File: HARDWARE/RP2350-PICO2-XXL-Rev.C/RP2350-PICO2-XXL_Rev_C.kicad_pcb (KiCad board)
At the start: 4 copper layers, 29 x 51 mm, 91 parts, among them Q1 Q12MHz/18pF/30ppm/4P/3.2x2.5m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, U1 W25Q128JVSIQ(SOIC-8_208mils), U2 TPS62A02ADRLR(SOT-563-6), U3 RP2350B(QFN-80_10.00x10.00x0.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, U4 NA(W25Q128JVSIQ(SOIC-8_208mil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, U5 APS6404L-3SQR-SN(SOIC-8_150mi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

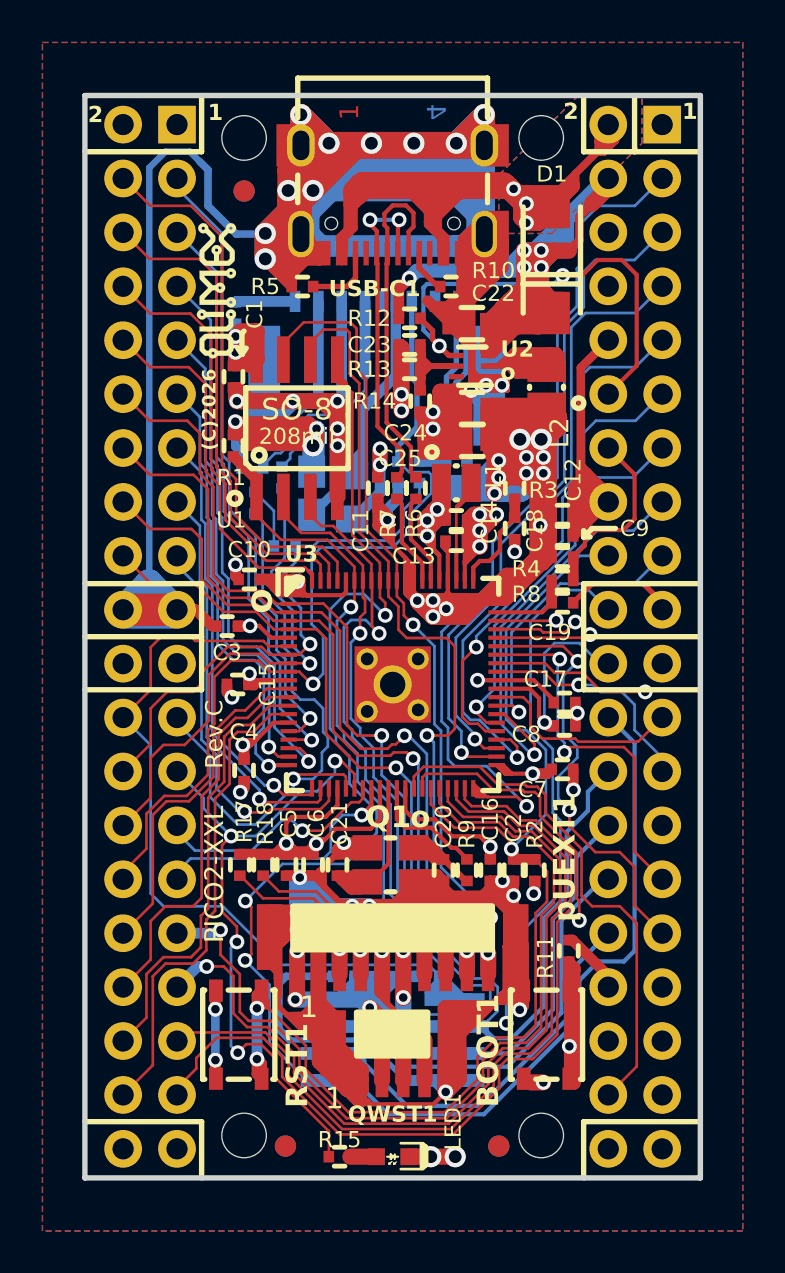
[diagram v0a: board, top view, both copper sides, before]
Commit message: removing unneeded connectors
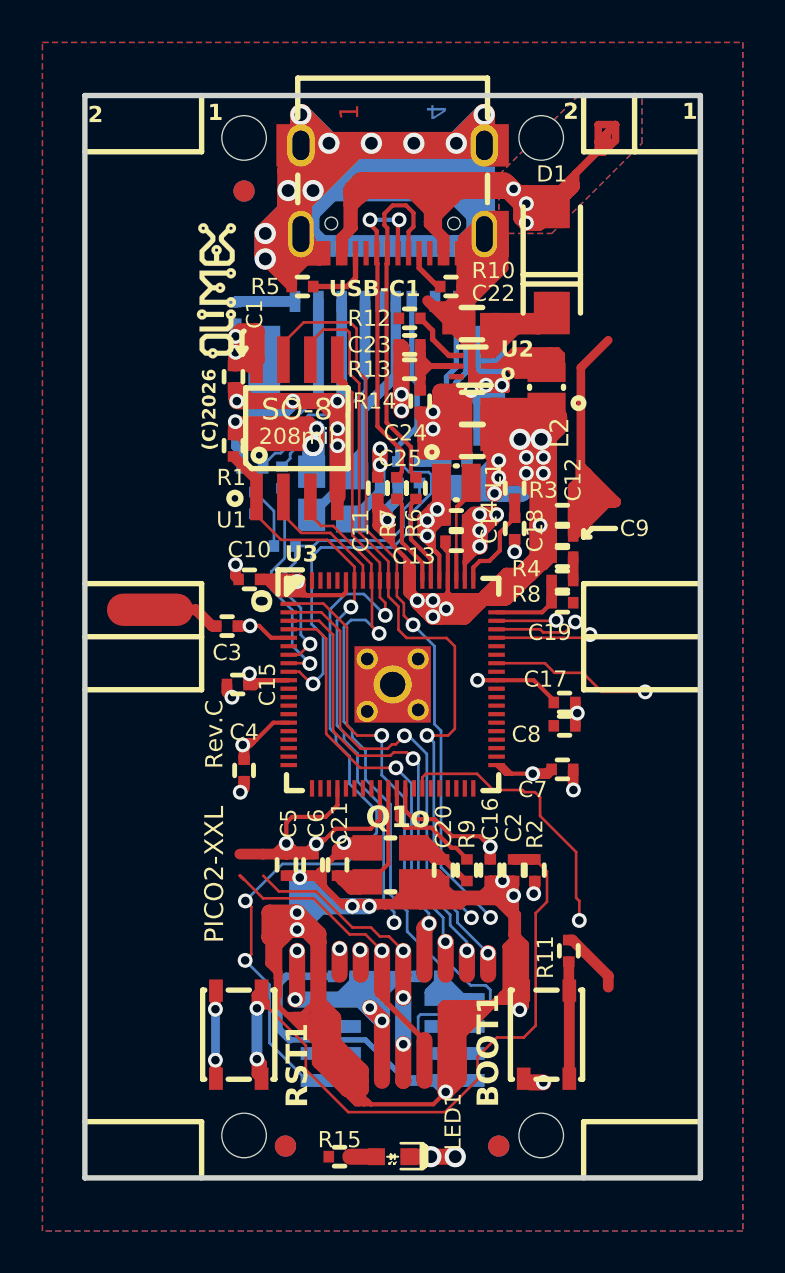
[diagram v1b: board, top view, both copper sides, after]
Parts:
- removed EXT1, EXT2: NA(HN2x20), OLIMEX_Connectors-FP:HN2x20
- removed QWST1: SH1.0-4P-180D, OLIMEX_Connectors-FP:BM04B-SRSS-TB
- removed R17, R18: 2.2k/R0402, OLIMEX_RLC-FP:R_0402_5MIL_DWS
- removed pUEXT1: SH1.0-10P-180D, OLIMEX_Connectors-FP:BM10B-SRSS-TB
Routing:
- net VSYS: track 62.9 -> 6.73 mm, vias 5 -> 0
- net /QSPI_SD1: track 52.0 -> 7.10 mm, vias 1 -> 0
- net /GPIO32: track 43.8 -> 0.00 mm, vias 1 -> 0
- net /BOOTSEL#: track 46.8 -> 5.53 mm, vias 2 -> 0
- net GND: track 634.6 -> 593.4 mm
- net /GPIO28: track 40.9 -> 0.00 mm, vias 1 -> 0
- net /GPIO29: track 40.2 -> 0.00 mm, vias 1 -> 0
- net /GPIO31: track 39.8 -> 0.00 mm
- net /GPIO30: track 38.0 -> 0.00 mm
- net /GPIO8\QMI_CS1n: track 40.1 -> 5.34 mm
- net /GPIO33: track 31.7 -> 0.00 mm, vias 1 -> 0
- net /GPIO25\User_Led: track 31.4 -> 0.00 mm, vias 4 -> 0
- net /QSPI_SD0: track 76.2 -> 46.0 mm
- net /GPIO16: track 29.5 -> 0.00 mm, vias 1 -> 0
- net /GPIO24\SPI1_RX\SD_DAT0: track 28.6 -> 0.00 mm, vias 1 -> 0
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
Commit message: cleaning up
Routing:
- net GND: track 593.4 -> 0.00 mm, vias 47 -> 0
- net +3.3V: track 385.8 -> 0.00 mm, vias 33 -> 0
- net /+1V1: track 112.2 -> 0.00 mm, vias 6 -> 0
- net VBUS: track 97.4 -> 0.00 mm, vias 3 -> 0
- net /GPIO3\I2C1_SCL: track 61.6 -> 0.00 mm, vias 1 -> 0
- net /GPIO2\I2C1_SDA: track 56.3 -> 0.00 mm, vias 3 -> 0
- net /GPIO47: track 47.5 -> 0.00 mm, vias 1 -> 0
- net /QSPI_SD0: track 46.0 -> 0.00 mm, vias 3 -> 0
- net /QSPI_CLK: track 44.1 -> 0.00 mm, vias 2 -> 0
- net /GPIO0\UART0_TX: track 44.0 -> 0.00 mm, vias 1 -> 0
- net /GPIO1\UART0_RX: track 43.7 -> 0.00 mm, vias 1 -> 0
- net /QSPI_CSn: track 42.0 -> 0.00 mm, vias 2 -> 0
- net /QSPI_SD3: track 41.7 -> 0.00 mm, vias 2 -> 0
- net /QSPI_SD2: track 38.7 -> 0.00 mm, vias 1 -> 0
- net /RUN: track 36.7 -> 0.00 mm, vias 2 -> 0
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
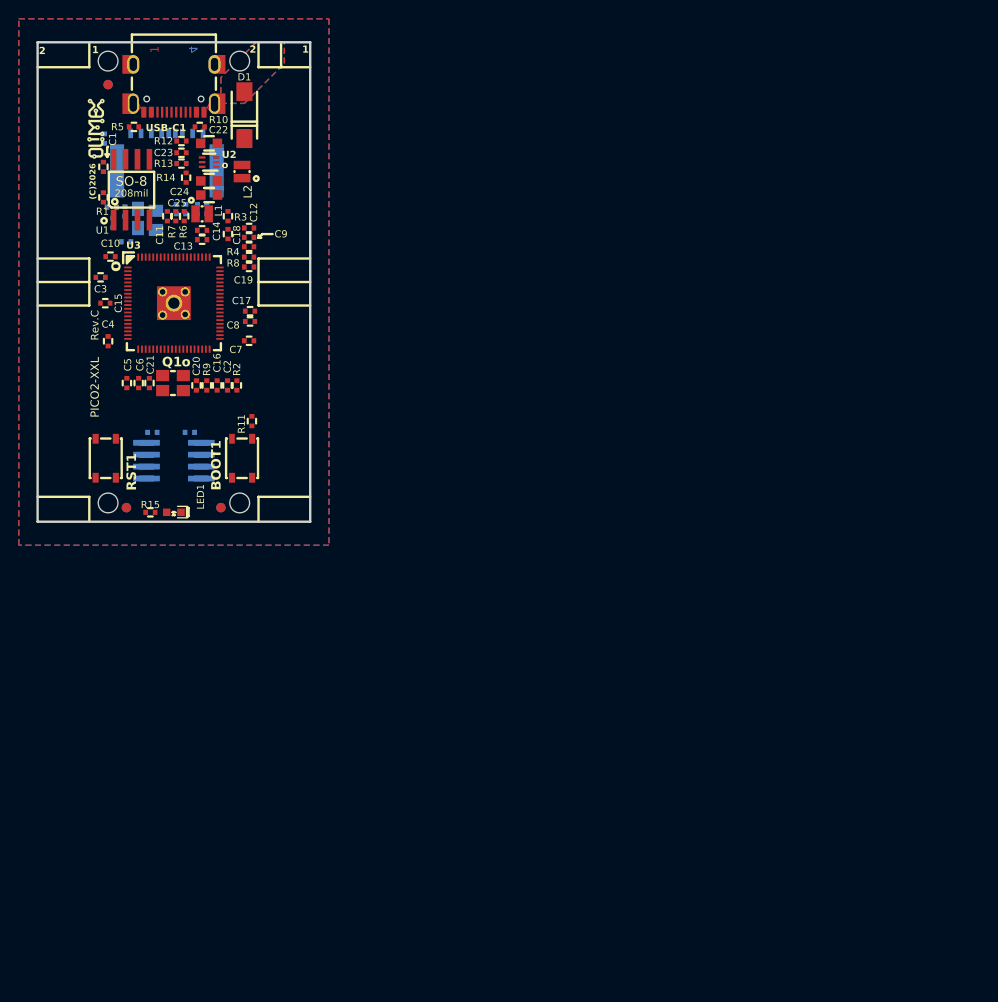
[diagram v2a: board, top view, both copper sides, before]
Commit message: 100x100 board outline
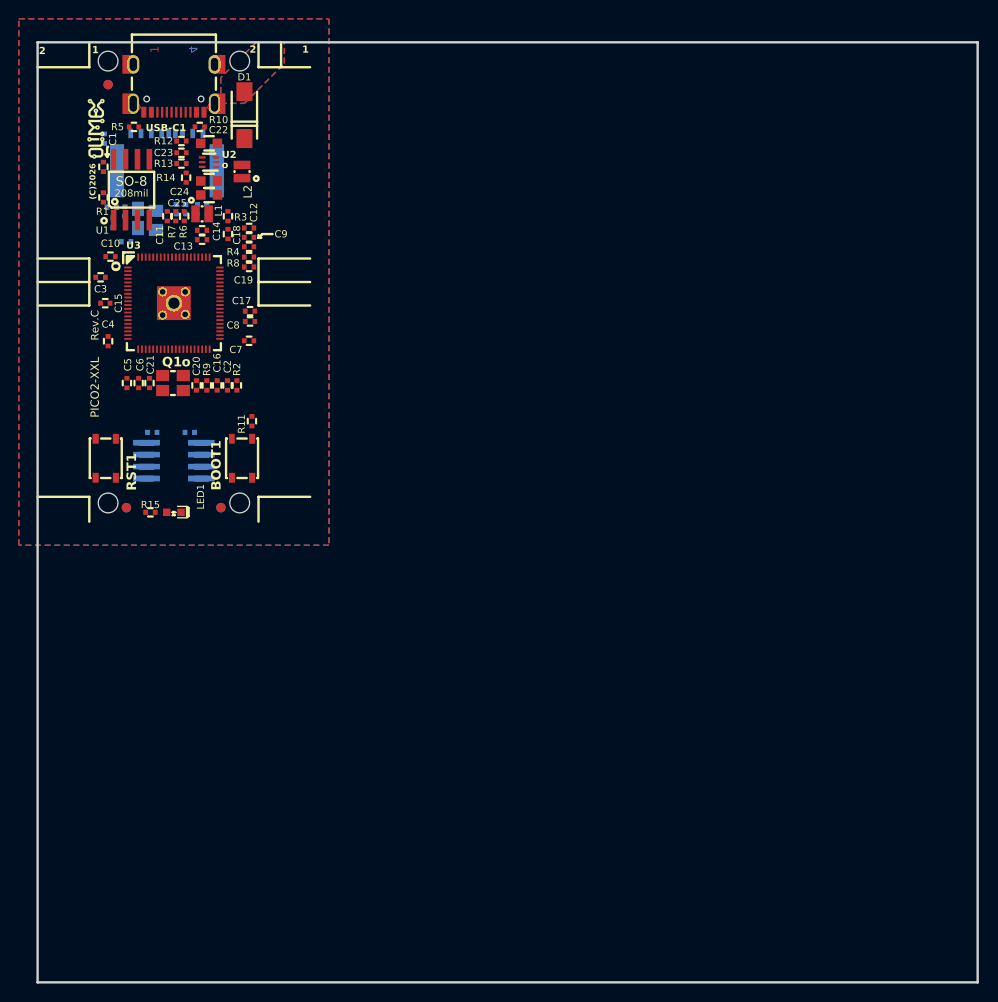
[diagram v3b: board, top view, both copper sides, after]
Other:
- board size 29 x 51 mm -> 100 x 100 mm
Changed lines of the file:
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@@
 	(gr_line
 		(start 136 64.5)
-		(end 165 64.5)
+		(end 236 64.5)
 		(stroke
 			(width 0.254)
@@
 	)
 	(gr_line
-		(start 136 115.5)
+		(start 136 164.5)
 		(end 136 64.5)
 		(stroke
@@
 	)
 	(gr_line
-		(start 136 115.5)
-		(end 165 115.5)
+		(start 136 164.5)
+		(end 236 164.5)
 		(stroke
 			(width 0.254)
@@
 	)
 	(gr_line
-		(start 165 115.5)
-		(end 165 64.5)
+		(start 236 164.5)
+		(end 236 64.5)
 		(stroke
 			(width 0.254)

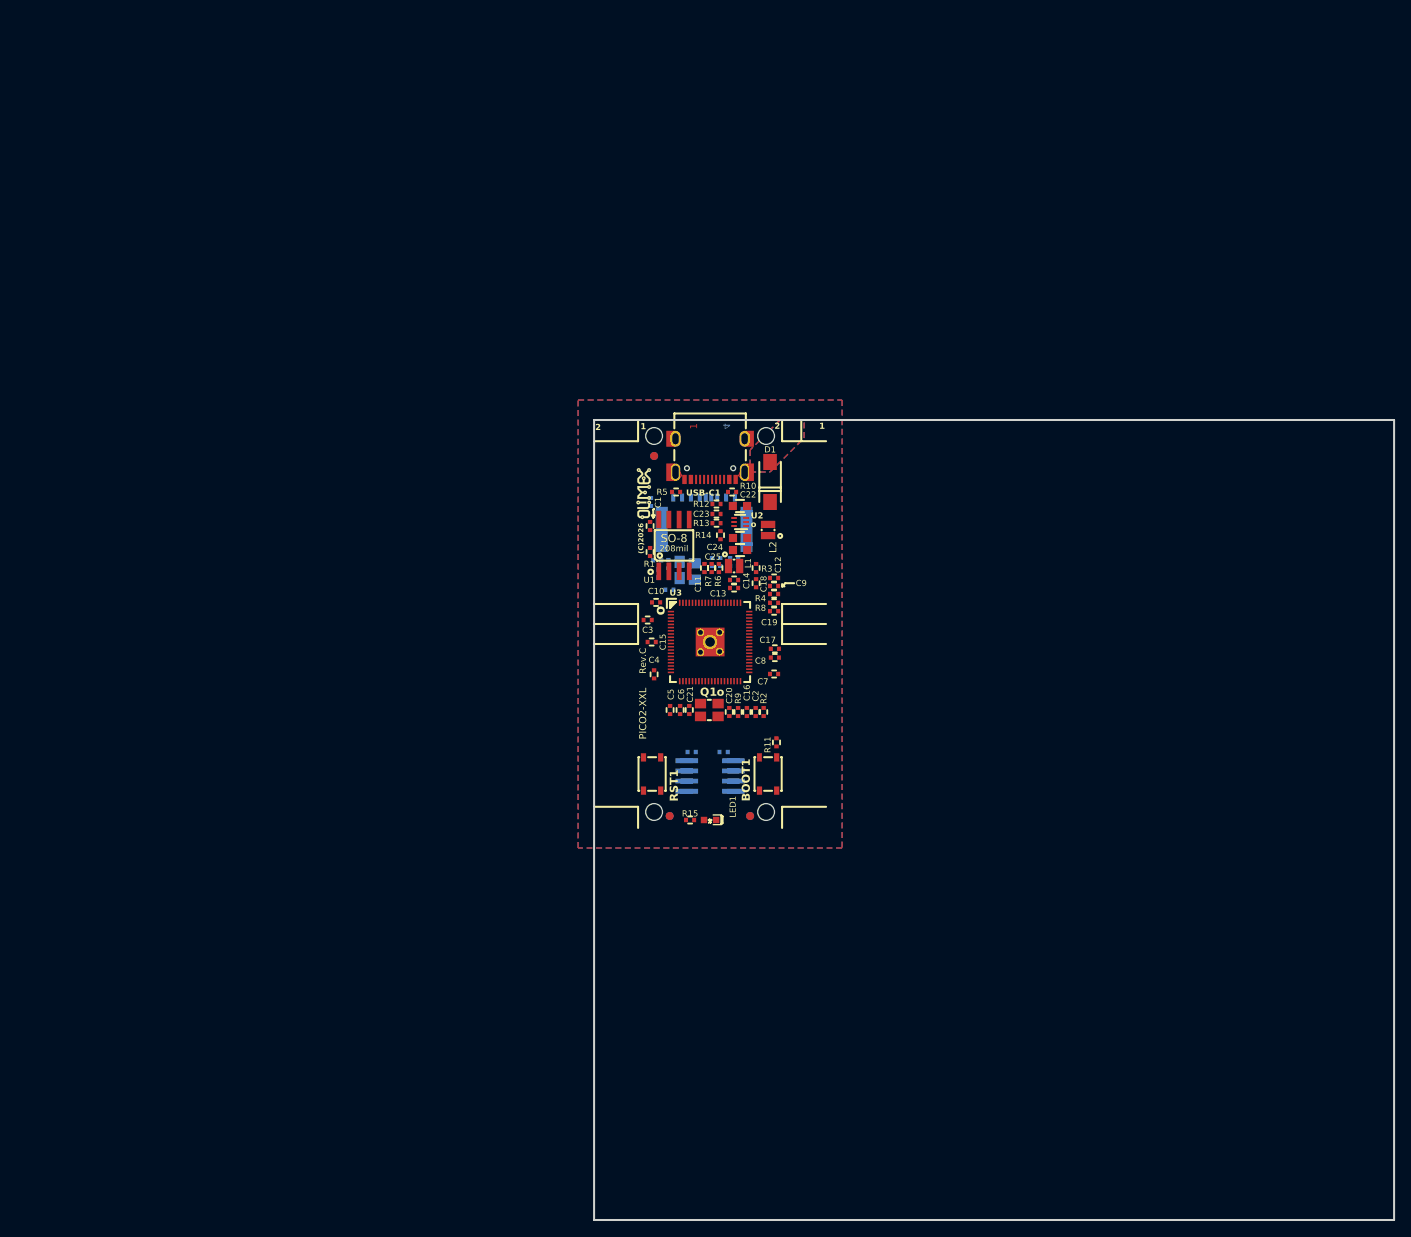
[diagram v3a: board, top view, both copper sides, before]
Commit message: routed psram and flash
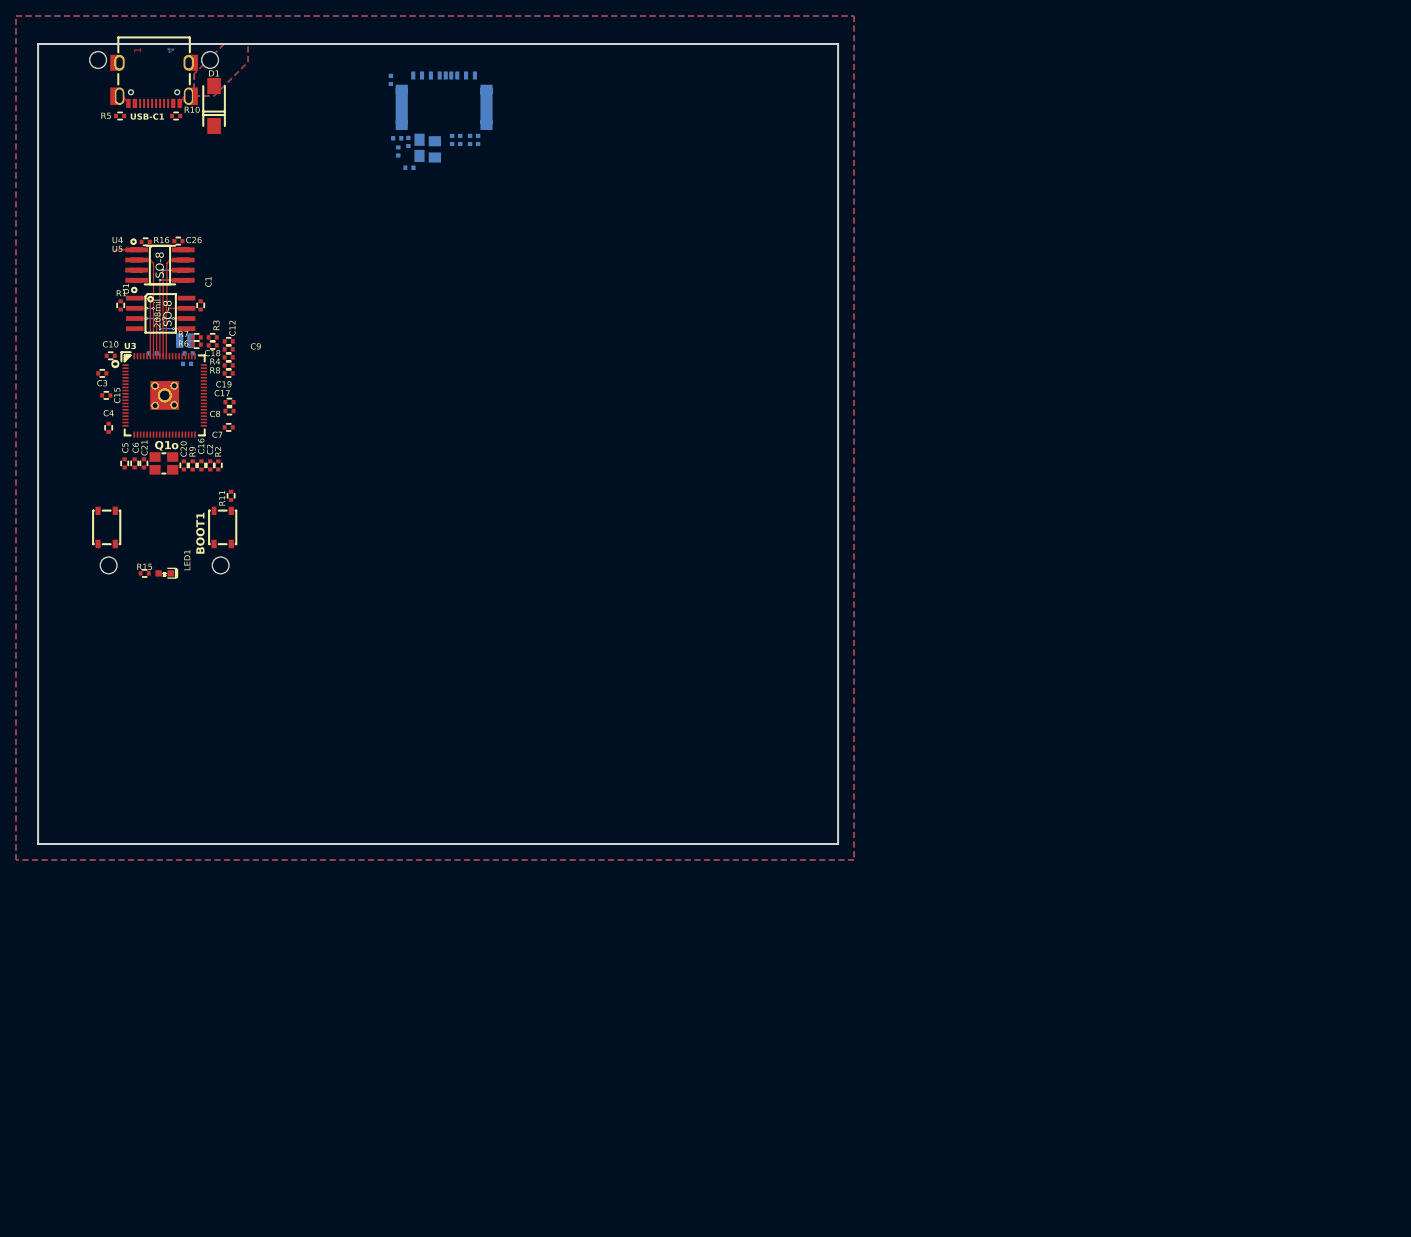
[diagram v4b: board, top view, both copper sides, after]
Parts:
- removed C22, C24: 22uF/6.3V/20%/X5R/C0603, OLIMEX_RLC-FP:C_0603_5MIL_DWS
- removed C23: NA(120pF/50V/5%/C0G/C0402), OLIMEX_RLC-FP:C_0402_5MIL_DWS
- removed C25: NA(22uF/6.3V/20%/X5R/C0603), OLIMEX_RLC-FP:C_0603_5MIL_DWS
- removed FID1, FID4: Fiducial, OLIMEX_Other-FP:Fiducial1x3_Paste
- removed FID2, FID3, FID5, FID6: Fiducial, OLIMEX_Other-FP:Fiducial1x3
- removed L2: 1.0uH/4.2A/DCR=35mR/20%/2.00x1.60x1.00mm/L2016(PIM201610-1R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, OLIMEX_RLC-FP:L_2016_MM
- removed Logo_OLIMEX_80, Logo_OLIMEX_80-Bot: Logo_OLIMEX_80, OLIMEX_Signs-FP:Logo_OLIMEX_80
- removed Logo_OLIMEX_TB: Logo_OLIMEX_TB, OLIMEX_Signs-FP:Logo_OLIMEX_TB
- removed R12: 1M/R0402, OLIMEX_RLC-FP:R_0402_5MIL_DWS
- removed R13: 220k/R0402, OLIMEX_RLC-FP:R_0402_5MIL_DWS
- removed R14: 49.9k/1%/R0402, OLIMEX_RLC-FP:R_0402_5MIL_DWS
- removed Sign_Antistatic_Small: Sign_Antistatic, OLIMEX_Signs-FP:Sign_Antistatic_4.5mmX2.8mm
- removed Sign_CE: CE_Sign, OLIMEX_Signs-FP:CE_Sign
- removed Sign_OSHW_7.3x6.0mm: Sign_OSHW_7.3x6.0mm, OLIMEX_Signs-FP:Sign_OSHW_7.3x6.0mmn
- removed Sign_PB-Free: Sign_PB-Free, OLIMEX_Signs-FP:Sign_PB-Free
- removed Sign_RecycleBin_1: Sign_RecycleBin_1, OLIMEX_Signs-FP:Sign_RecycleBin_1
- removed U2: TPS62A02ADRLR(SOT-563-6), OLIMEX_Regulators-FP:SOT-563-6
- C11, C13, C14, L1: moved to B.Cu
- C26, R16, U4, U5: moved to F.Cu
- moved R16 96.4 mm to (79.9, 42.2), turned to 180 degrees
- moved U4 93.8 mm to (81.7, 45.1)
- moved U5 93.8 mm to (81.7, 45.1)
- moved C26 90.5 mm to (84.0, 42.1), turned to 180 degrees
- moved D1 83.9 mm to (88.5, 25.2)
- moved MH3 83.9 mm to (74.0, 19.5)
- moved MH4 83.9 mm to (88.0, 19.5)
- moved R10 83.9 mm to (83.8, 26.5)
- moved R5 83.9 mm to (76.8, 26.5)
- moved USB-C1 83.9 mm to (81.0, 21.0)
- moved C20 74.8 mm to (84.7, 70.2)
- moved C21 74.8 mm to (79.7, 69.9)
- moved Q1 74.8 mm to (82.2, 69.9)
- moved R11 74.8 mm to (90.6, 74.0)
- moved BOOT1 74.8 mm to (89.6, 77.9)
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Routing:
- net /QSPI_SD3: track 0.00 -> 16.3 mm
- net /QSPI_SD1: track 0.00 -> 15.9 mm, vias 0 -> 2
- net /QSPI_CLK: track 0.00 -> 15.9 mm, vias 0 -> 4
- net /QSPI_SD0: track 0.00 -> 15.5 mm, vias 0 -> 4
- net /QSPI_CSn: track 0.00 -> 9.02 mm
- net /QSPI_SD2: track 0.00 -> 7.45 mm, vias 0 -> 2
- net /GPIO8\QMI_CS1n: track 0.00 -> 3.25 mm
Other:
- board text removed: "(C)2026"
- board text removed: "PICO2-XXL"
- board text removed: "Rev.C"
- board text removed: "RoHS Compliant"
- board text removed: "www.olimex.com"
